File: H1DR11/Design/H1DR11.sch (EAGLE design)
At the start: 34 parts, among them P1 HEXABIT_17.32_NO_P6, U1 STM32F091CBU6, U2 MAX14840EASAT, X1 XTALL_CSTCE8M00G52

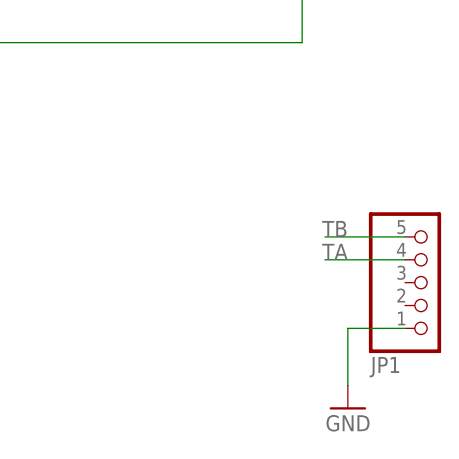
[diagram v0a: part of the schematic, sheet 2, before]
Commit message: mirror pin header
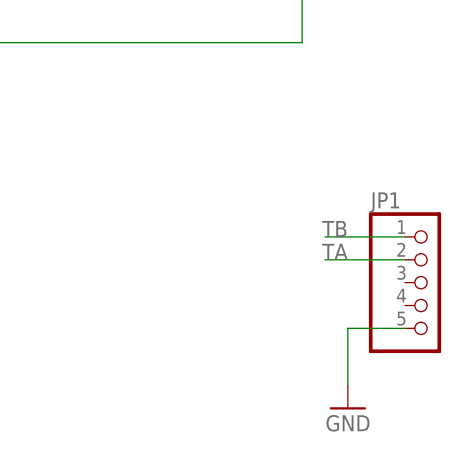
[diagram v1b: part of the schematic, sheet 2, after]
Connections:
- net GND: now also JP1.5; no longer JP1.1
- net TA: now also JP1.2; no longer JP1.4
- net TB: now also JP1.1; no longer JP1.5
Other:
- moved on the sheet: JP1
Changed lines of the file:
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@@
 <attribute name="VALUE" x="237.49" y="53.34" size="1.778" layer="96" rot="MR0"/>
 </instance>
-<instance part="JP1" gate="A" x="243.84" y="69.85" smashed="yes" rot="MR180">
-<attribute name="NAME" x="237.49" y="61.595" size="1.778" layer="95" rot="MR180"/>
-<attribute name="VALUE" x="237.49" y="80.01" size="1.778" layer="96" rot="MR180"/>
+<instance part="JP1" gate="A" x="243.84" y="69.85" smashed="yes">
+<attribute name="NAME" x="237.49" y="78.105" size="1.778" layer="95"/>
+<attribute name="VALUE" x="237.49" y="59.69" size="1.778" layer="96"/>
 </instance>
 </instances>
@@
 <wire x1="234.95" y1="64.77" x2="234.95" y2="58.42" width="0.1524" layer="91"/>
 <pinref part="GND16" gate="1" pin="GND"/>
-<pinref part="JP1" gate="A" pin="1"/>
+<pinref part="JP1" gate="A" pin="5"/>
 </segment>
 </net>
@@
 <wire x1="241.3" y1="74.93" x2="232.41" y2="74.93" width="0.1524" layer="91"/>
 <label x="234.95" y="74.93" size="1.778" layer="95" rot="MR0"/>
-<pinref part="JP1" gate="A" pin="5"/>
+<pinref part="JP1" gate="A" pin="1"/>
 </segment>
 </net>
@@
 <wire x1="241.3" y1="72.39" x2="232.41" y2="72.39" width="0.1524" layer="91"/>
 <label x="234.95" y="72.39" size="1.778" layer="95" rot="MR0"/>
-<pinref part="JP1" gate="A" pin="4"/>
+<pinref part="JP1" gate="A" pin="2"/>
 </segment>
 </net>

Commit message: 3way terminal block  was added
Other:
- note added: "H1DR1"
- note removed: "H1DR11"
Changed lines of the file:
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@@
 <text x="215.9" y="5.3848" size="1.9304" layer="100" font="vector">Sheet   of</text>
 <text x="199.4662" y="19.6342" size="1.9304" layer="100" font="vector">Title</text>
-<text x="180.9242" y="19.6342" size="1.9304" layer="102" font="vector">H1DR11</text>
+<text x="180.9242" y="19.6342" size="1.9304" layer="102" font="vector">H1DR1</text>
 <text x="191.9478" y="11.2014" size="1.9304" layer="101" font="vector" align="center">RS485 Serial Transceiver</text>
 <text x="206.3242" y="19.6342" size="1.9304" layer="101" font="vector">H1DR11_Backend</text>
@@
 <text x="215.9" y="5.3848" size="1.9304" layer="100" font="vector">Sheet   of</text>
 <text x="199.4662" y="19.6342" size="1.9304" layer="100" font="vector">Title</text>
-<text x="180.9242" y="19.6342" size="1.9304" layer="102" font="vector">H1DR11</text>
+<text x="180.9242" y="19.6342" size="1.9304" layer="102" font="vector">H1DR1</text>
 <text x="206.3242" y="19.6342" size="1.9304" layer="101" font="vector">H1DR11_Frontend</text>
 <wire x1="168.91" y1="3.81" x2="168.91" y2="8.128" width="0.1524" layer="205"/>

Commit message: output CAM files generated
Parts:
- JP1: DESCRIPTION (none) -> Conn Header R/a 5POS 2.54MM MALE; MFN (none) -> Sullins; MPN (none) -> PEC05SBAN; OCTOPART_URL (none) -> https://octopart.com/pec05sban-sullins-264498?r=sp
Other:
- moved on the sheet: JP1
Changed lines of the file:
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@@
 <?xml version="1.0" encoding="utf-8"?>
 <!DOCTYPE eagle SYSTEM "eagle.dtd">
-<eagle version="9.6.0">
+<eagle version="9.6.1">
 <drawing>
 <settings>
@@
 <setting verticaltext="up"/>
 </settings>
-<grid distance="50" unitdist="mil" unit="mil" style="lines" multiple="1" display="yes" altdistance="0.01" altunitdist="inch" altunit="inch"/>
+<grid distance="0.1" unitdist="inch" unit="inch" style="lines" multiple="1" display="no" altdistance="0.01" altunitdist="inch" altunit="inch"/>
 <layers>
 <layer number="1" name="Top" color="4" fill="1" visible="no" active="no"/>
@@
 </part>
 <part name="GND16" library="supply1" library_urn="urn:adsk.eagle:library:371" deviceset="GND" device=""/>
-<part name="JP1" library="Hexabitz" deviceset="PINHD-1X5" device="/90" package3d_urn="urn:adsk.eagle:package:22467/2"/>
+<part name="JP1" library="Hexabitz" deviceset="PINHD-1X5" device="/90" package3d_urn="urn:adsk.eagle:package:22467/2">
+<attribute name="DESCRIPTION" value="Conn Header R/a 5POS 2.54MM MALE"/>
+<attribute name="MFN" value="Sullins"/>
+<attribute name="MPN" value="PEC05SBAN"/>
+<attribute name="OCTOPART_URL" value="https://octopart.com/pec05sban-sullins-264498?r=sp"/>
+</part>
 </parts>
 <sheets>
@@
 <attribute name="VALUE" x="204.47" y="110.998" size="1.778" layer="96"/>
 </instance>
-<instance part="GND16" gate="1" x="234.95" y="55.88" smashed="yes" rot="MR0">
-<attribute name="VALUE" x="237.49" y="53.34" size="1.778" layer="96" rot="MR0"/>
+<instance part="GND16" gate="1" x="49.53" y="33.02" smashed="yes">
+<attribute name="VALUE" x="46.99" y="30.48" size="1.778" layer="96"/>
 </instance>
-<instance part="JP1" gate="A" x="243.84" y="69.85" smashed="yes">
-<attribute name="NAME" x="237.49" y="78.105" size="1.778" layer="95"/>
-<attribute name="VALUE" x="237.49" y="59.69" size="1.778" layer="96"/>
+<instance part="JP1" gate="A" x="40.64" y="46.99" smashed="yes" rot="MR0">
+<attribute name="NAME" x="46.99" y="55.245" size="1.778" layer="95" rot="MR0"/>
+<attribute name="VALUE" x="46.99" y="36.83" size="1.778" layer="96" rot="MR0"/>
+<attribute name="DESCRIPTION" x="40.64" y="46.99" size="1.778" layer="96" rot="MR0" display="off"/>
+<attribute name="MFN" x="40.64" y="46.99" size="1.778" layer="96" rot="MR0" display="off"/>
+<attribute name="MPN" x="40.64" y="46.99" size="1.778" layer="96" rot="MR0" display="off"/>
+<attribute name="OCTOPART_URL" x="40.64" y="46.99" size="1.778" layer="96" rot="MR0" display="off"/>
 </instance>
 </instances>
@@
 </segment>
 <segment>
-<wire x1="241.3" y1="64.77" x2="234.95" y2="64.77" width="0.1524" layer="91"/>
-<wire x1="234.95" y1="64.77" x2="234.95" y2="58.42" width="0.1524" layer="91"/>
+<wire x1="43.18" y1="41.91" x2="49.53" y2="41.91" width="0.1524" layer="91"/>
+<wire x1="49.53" y1="41.91" x2="49.53" y2="35.56" width="0.1524" layer="91"/>
 <pinref part="GND16" gate="1" pin="GND"/>
 <pinref part="JP1" gate="A" pin="5"/>
@@
 </segment>
 <segment>
-<wire x1="241.3" y1="74.93" x2="232.41" y2="74.93" width="0.1524" layer="91"/>
-<label x="234.95" y="74.93" size="1.778" layer="95" rot="MR0"/>
+<wire x1="43.18" y1="52.07" x2="52.07" y2="52.07" width="0.1524" layer="91"/>
+<label x="49.53" y="52.07" size="1.778" layer="95"/>
 <pinref part="JP1" gate="A" pin="1"/>
 </segment>
@@
 </segment>
 <segment>
-<wire x1="241.3" y1="72.39" x2="232.41" y2="72.39" width="0.1524" layer="91"/>
-<label x="234.95" y="72.39" size="1.778" layer="95" rot="MR0"/>
+<wire x1="43.18" y1="49.53" x2="52.07" y2="49.53" width="0.1524" layer="91"/>
+<label x="49.53" y="49.53" size="1.778" layer="95"/>
 <pinref part="JP1" gate="A" pin="2"/>
 </segment>
